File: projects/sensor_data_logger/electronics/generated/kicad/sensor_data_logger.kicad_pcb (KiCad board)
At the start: 2 copper layers, 70 x 50 mm, 20 parts, among them J1 USB-C POWER, J2 UART DEBUG, Q1 Ideal Diode, U1 ESP32-S3-WROOM-1, U2 ICM-42688-P, U3 3V3 Buck

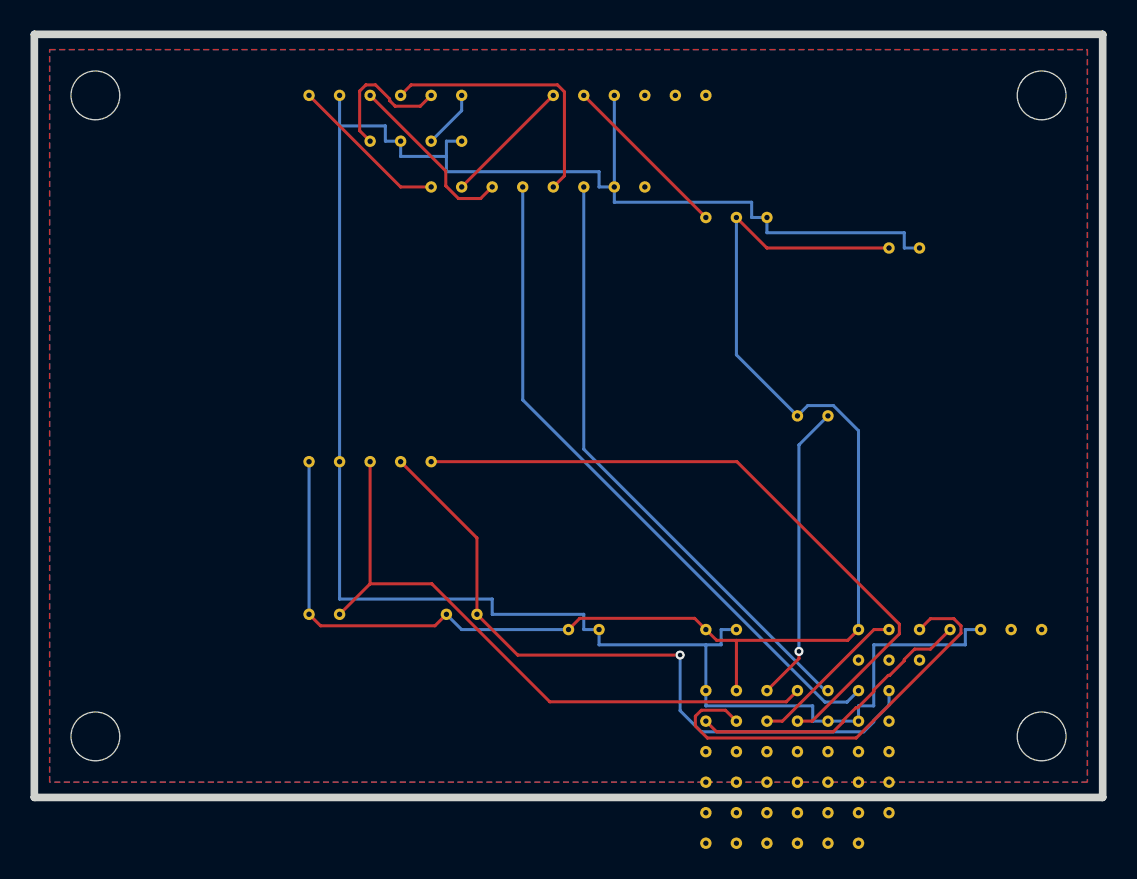
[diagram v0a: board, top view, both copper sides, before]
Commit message: feat: add isolated jobs and mini robot design flow
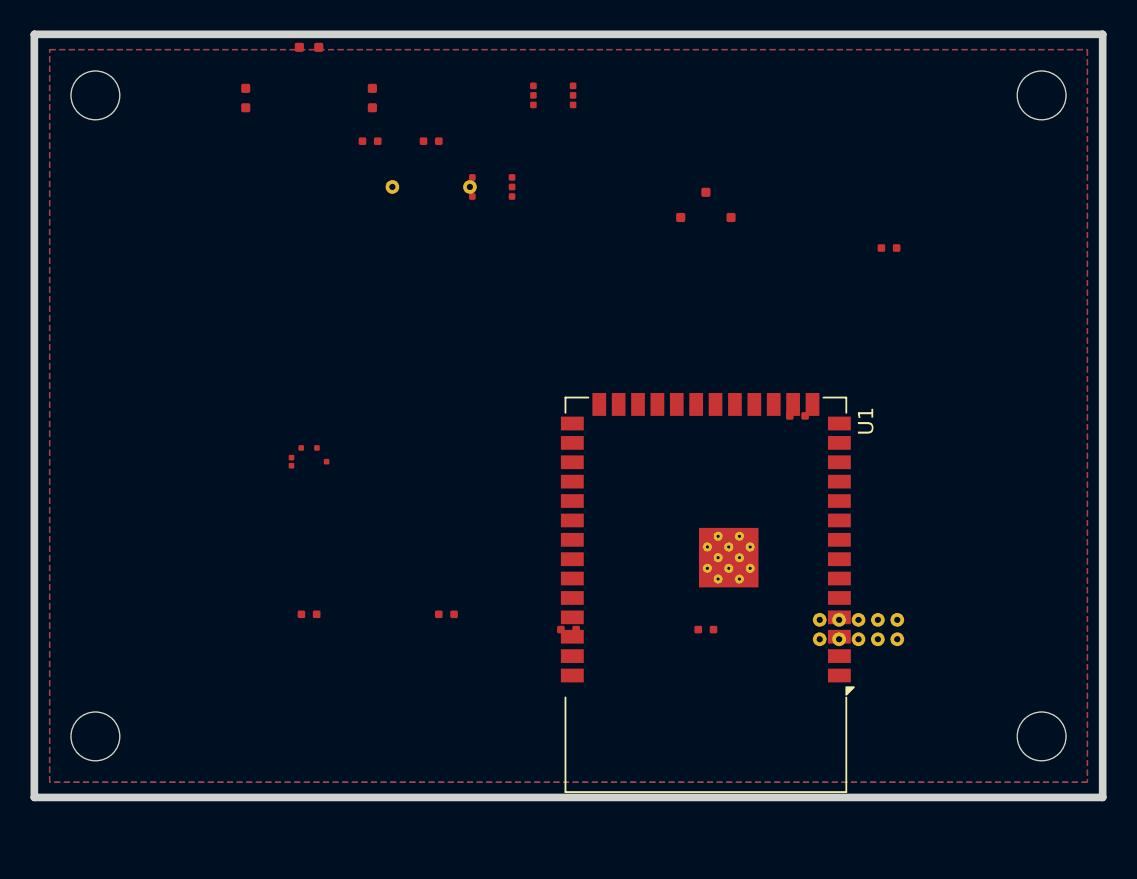
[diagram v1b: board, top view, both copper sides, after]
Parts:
- moved U1 6.25 mm to (44.0, 36.7), turned to 180 degrees
- moved J1 0.18 mm to (18.0, 4.18)
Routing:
- net GND: track 146.0 -> 0.00 mm
- net V3V3: track 95.0 -> 0.00 mm
- net I2C_IMU_SDA: track 46.1 -> 0.00 mm, vias 1 -> 0
- net IMU_INT: track 44.8 -> 0.00 mm
- net USB_DP: track 44.5 -> 0.00 mm
- net I2C_IMU_SCL: track 42.3 -> 0.00 mm
- net USB_DM: track 39.7 -> 0.00 mm
- net UART_RX: track 28.1 -> 0.00 mm
- net ESP_EN: track 19.7 -> 0.00 mm, vias 1 -> 0
- net BOOT: track 19.2 -> 0.00 mm
- net USB_DM_RAW: track 17.7 -> 0.00 mm
- net USB_DP_RAW: track 11.7 -> 0.00 mm
- net USB_PROT: track 11.3 -> 0.00 mm
- net USB_VBUS: track 10.5 -> 0.00 mm
- net UART_TX: track 10.5 -> 0.00 mm
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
